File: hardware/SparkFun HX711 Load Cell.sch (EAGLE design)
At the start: 27 parts, among them Q1 MMBT4403, U1 HX711, U7 OSHW-LOGOS

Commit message: Fixing issues #6.
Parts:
- FRAME1: value FRAME-LETTER -> (none); DESIGNER (none) -> N. Seidle; VERSION (none) -> v10
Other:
- note removed: "20k 8.2k"
- note removed: "N. Seidle"
- note removed: "v01"
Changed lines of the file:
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@@
 </classes>
 <parts>
-<part name="FRAME1" library="SparkFun-Aesthetics" deviceset="FRAME-LETTER" device=""/>
 <part name="U7" library="SparkFun-Aesthetics" deviceset="OSHW-LOGO" device="S"/>
 <part name="STANDOFF1" library="SparkFun-Electromechanical" deviceset="STAND-OFF" device=""/>
@@
 <part name="GND6" library="SparkFun-Aesthetics" deviceset="GND" device=""/>
 <part name="GND9" library="SparkFun-Aesthetics" deviceset="GND" device=""/>
+<part name="FRAME1" library="SparkFun-Aesthetics" deviceset="FRAME-LETTER" device="">
+<attribute name="DESIGNER" value="N. Seidle"/>
+<attribute name="VERSION" value="v10"/>
+</part>
 </parts>
 <sheets>
@@
 <text x="10.414" y="128.016" size="1.778" layer="97">Common Load
 Cell Colors:</text>
-<text x="172.72" y="10.16" size="2.54" layer="94">N. Seidle</text>
-<text x="238.76" y="7.62" size="2.54" layer="94">v01</text>
 <text x="213.36" y="99.06" size="1.778" layer="97">IO: 2.7-5.5V</text>
 <text x="38.1" y="114.3" size="1.778" layer="97">Shield</text>
@@
 <wire x1="36.576" y1="127" x2="40.64" y2="127" width="0.2032" layer="97"/>
 <wire x1="36.576" y1="113.03" x2="40.64" y2="113.03" width="0.2032" layer="97"/>
-<text x="63.5" y="144.78" size="1.778" layer="91">20k 8.2k</text>
 </plain>
 <instances>
-<instance part="FRAME1" gate="G$1" x="0" y="0"/>
-<instance part="FRAME1" gate="G$2" x="147.32" y="0"/>
 <instance part="U7" gate="G$1" x="132.08" y="12.7"/>
 <instance part="STANDOFF1" gate="G$1" x="243.84" y="38.1"/>
@@
 <instance part="GND6" gate="1" x="91.44" y="109.22"/>
 <instance part="GND9" gate="1" x="119.38" y="88.9"/>
+<instance part="FRAME1" gate="G$1" x="0" y="0"/>
+<instance part="FRAME1" gate="V" x="147.32" y="0"/>
 </instances>
 <busses>

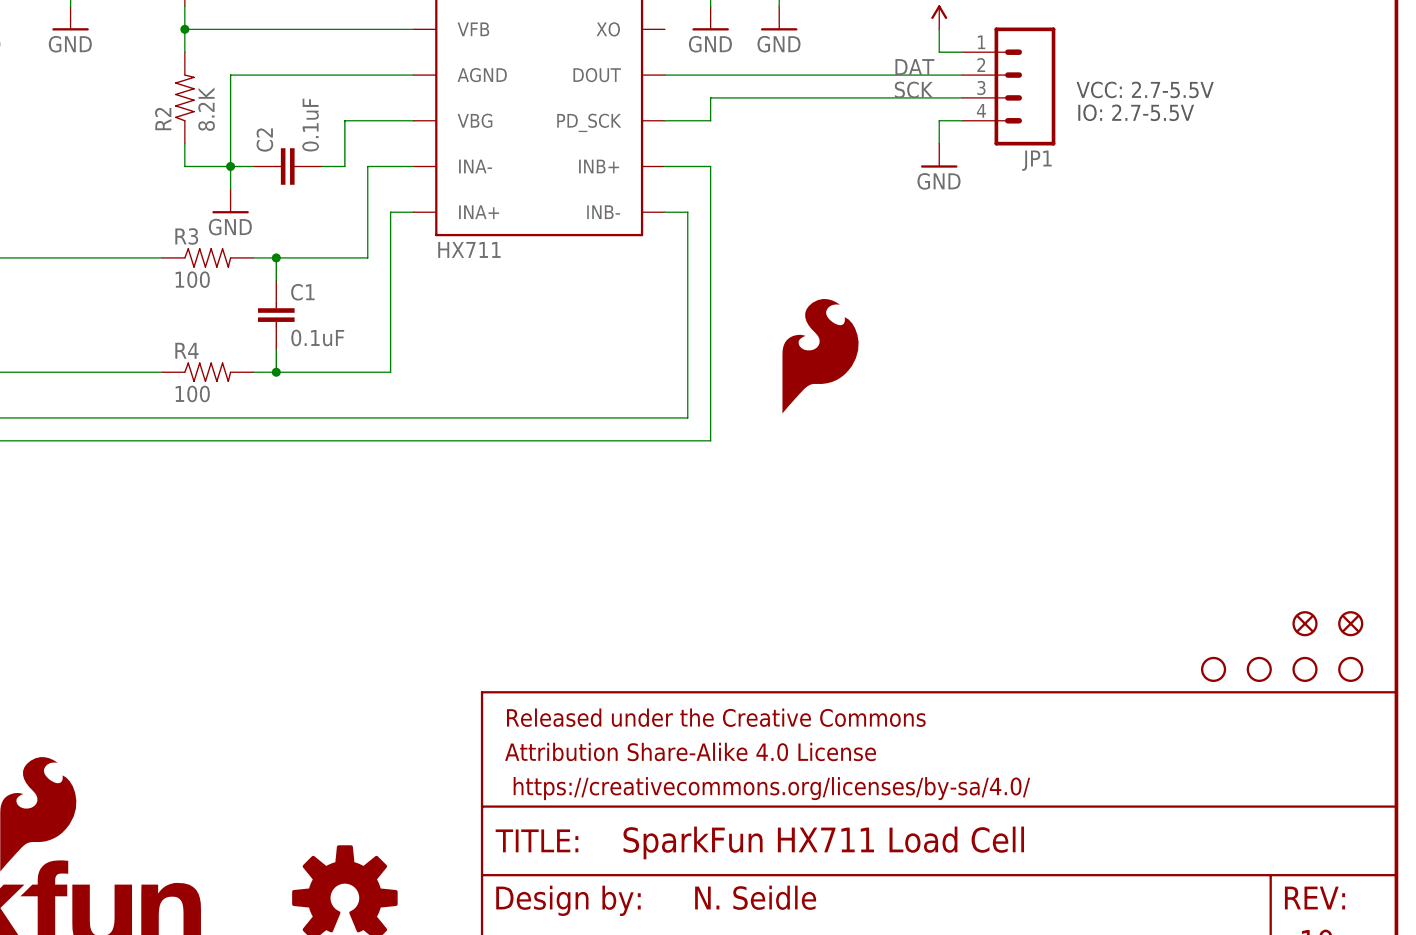
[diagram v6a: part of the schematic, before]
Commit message: Fixed feedback from eng review.
Moved VCC trace out of tKeepout. Fixed 4-way junction on schematic.
Moved schematic part for standoff holes to proper location.
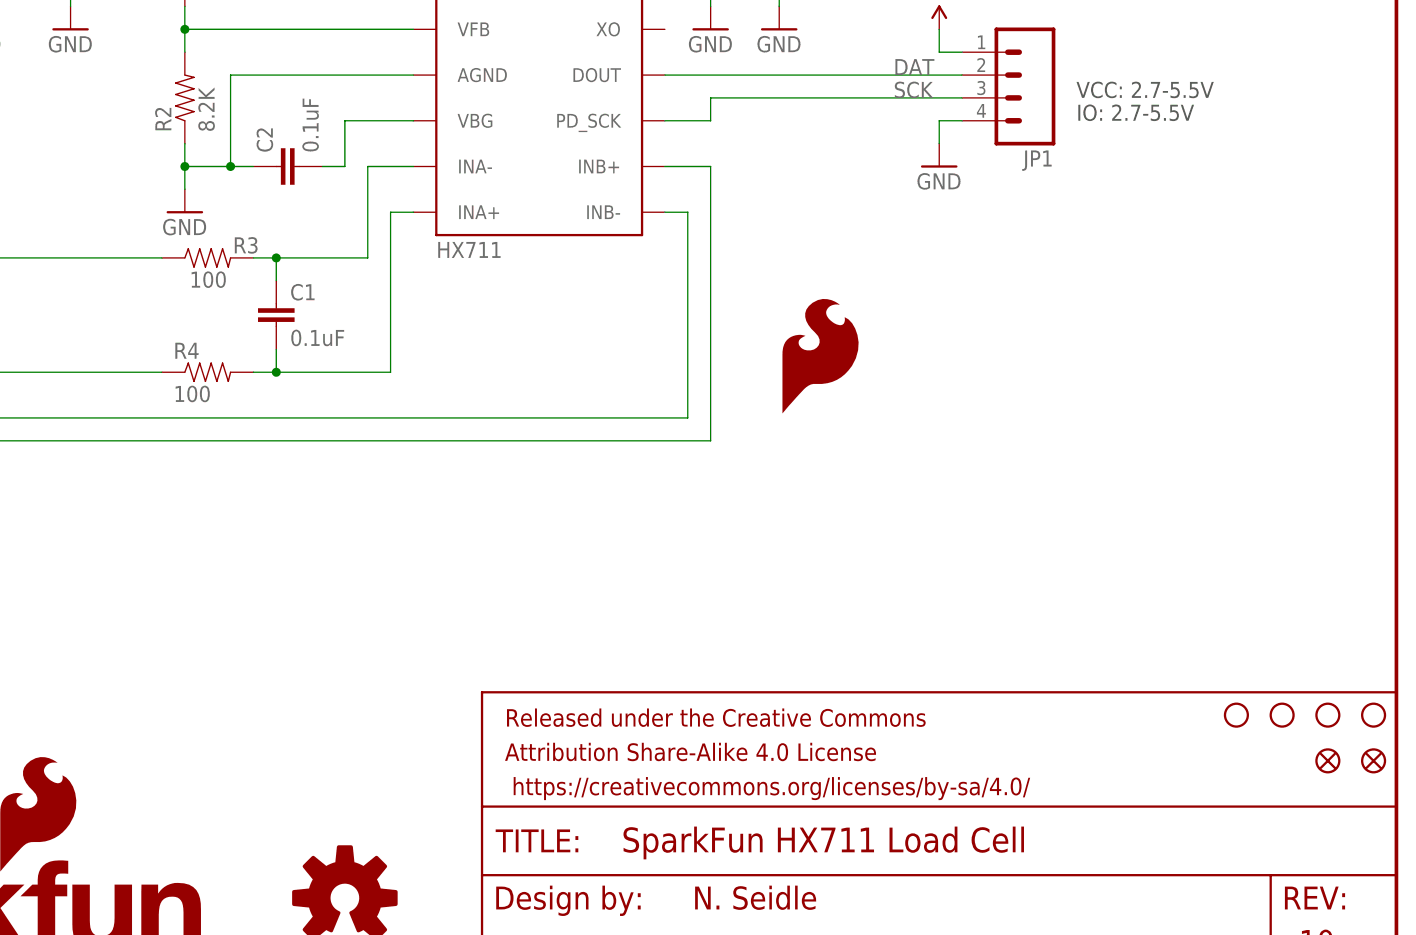
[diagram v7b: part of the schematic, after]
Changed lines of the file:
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@@
 <?xml version="1.0" encoding="utf-8"?>
 <!DOCTYPE eagle SYSTEM "eagle.dtd">
-<eagle version="7.1.0">
+<eagle version="7.2.0">
 <drawing>
 <settings>
@@
 <layer number="255" name="routoute" color="7" fill="1" visible="yes" active="yes"/>
 </layers>
-<schematic xreflabel="%F%N/%S.%C%R" xrefpart="/%S.%C%R">
+<schematic xreflabel="%F%N/%S" xrefpart="/%S.%C%R">
 <attributes>
 </attributes>
@@
 <instances>
 <instance part="U7" gate="G$1" x="132.08" y="12.7"/>
-<instance part="STANDOFF1" gate="G$1" x="243.84" y="38.1"/>
-<instance part="STANDOFF2" gate="G$1" x="238.76" y="38.1"/>
-<instance part="STANDOFF3" gate="G$1" x="233.68" y="38.1"/>
-<instance part="STANDOFF4" gate="G$1" x="228.6" y="38.1"/>
+<instance part="STANDOFF1" gate="G$1" x="246.38" y="33.02"/>
+<instance part="STANDOFF2" gate="G$1" x="241.3" y="33.02"/>
+<instance part="STANDOFF3" gate="G$1" x="236.22" y="33.02"/>
+<instance part="STANDOFF4" gate="G$1" x="231.14" y="33.02"/>
 <instance part="LOGO1" gate="G$1" x="60.96" y="2.54"/>
 <instance part="JP1" gate="G$1" x="205.74" y="104.14" rot="R180"/>
@@
 <instance part="Q1" gate="G$1" x="121.92" y="132.08" rot="MR0"/>
 <instance part="GND1" gate="1" x="198.12" y="93.98"/>
-<instance part="R3" gate="G$1" x="116.84" y="83.82"/>
+<instance part="R3" gate="G$1" x="116.84" y="83.82" smashed="yes">
+<attribute name="NAME" x="119.634" y="84.328" size="1.778" layer="95"/>
+<attribute name="VALUE" x="114.808" y="80.518" size="1.778" layer="96"/>
+</instance>
 <instance part="R4" gate="G$1" x="116.84" y="71.12"/>
 <instance part="C6" gate="G$1" x="106.68" y="144.78"/>
@@
 <instance part="GND8" gate="1" x="91.44" y="137.16"/>
 <instance part="LOGO3" gate="G$1" x="180.34" y="66.04"/>
-<instance part="FID1" gate="G$1" x="243.84" y="43.18"/>
-<instance part="FID2" gate="G$1" x="238.76" y="43.18"/>
+<instance part="FID1" gate="G$1" x="246.38" y="27.94"/>
+<instance part="FID2" gate="G$1" x="241.3" y="27.94"/>
 <instance part="JP2" gate="G$1" x="50.8" y="99.06"/>
 <instance part="SJ2" gate="G$1" x="180.34" y="119.38" rot="R90"/>
@@
 <instance part="C3" gate="G$1" x="91.44" y="116.84"/>
 <instance part="GND6" gate="1" x="91.44" y="109.22"/>
-<instance part="GND9" gate="1" x="119.38" y="88.9"/>
+<instance part="GND9" gate="1" x="114.3" y="88.9"/>
 <instance part="FRAME1" gate="G$1" x="0" y="0"/>
 <instance part="FRAME1" gate="V" x="147.32" y="0"/>
@@
 <pinref part="C2" gate="G$1" pin="1"/>
 <pinref part="GND9" gate="1" pin="GND"/>
-<wire x1="119.38" y1="93.98" x2="119.38" y2="91.44" width="0.1524" layer="91"/>
-</segment>
-<segment>
+<wire x1="114.3" y1="91.44" x2="114.3" y2="93.98" width="0.1524" layer="91"/>
+<junction x="114.3" y="93.98"/>
+</segment>
+<segment>

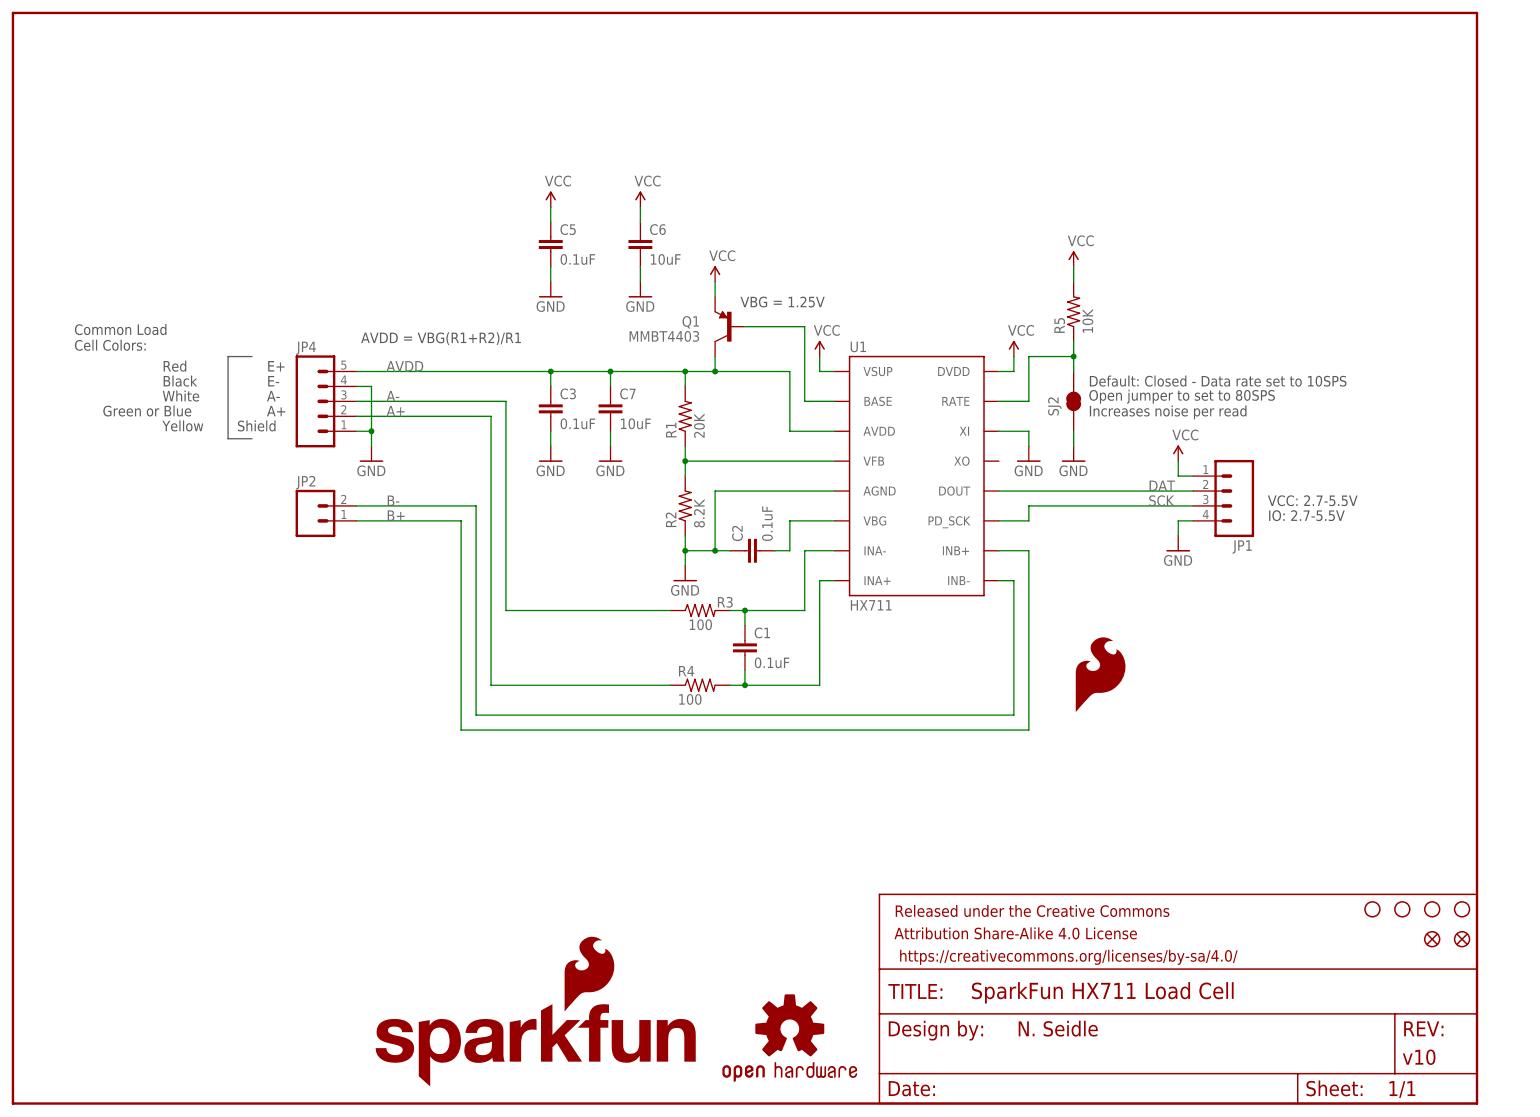
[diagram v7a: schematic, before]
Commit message: Revision 11 changes
-Added 3.3uH inductor, this should allow for greater resolution in the
HX711 ADC.
-Separated analog and digital supply voltage, which allows 3.3V uCs to
communicate without additional hardware.
-Added 0.1uF cap to digital supply.
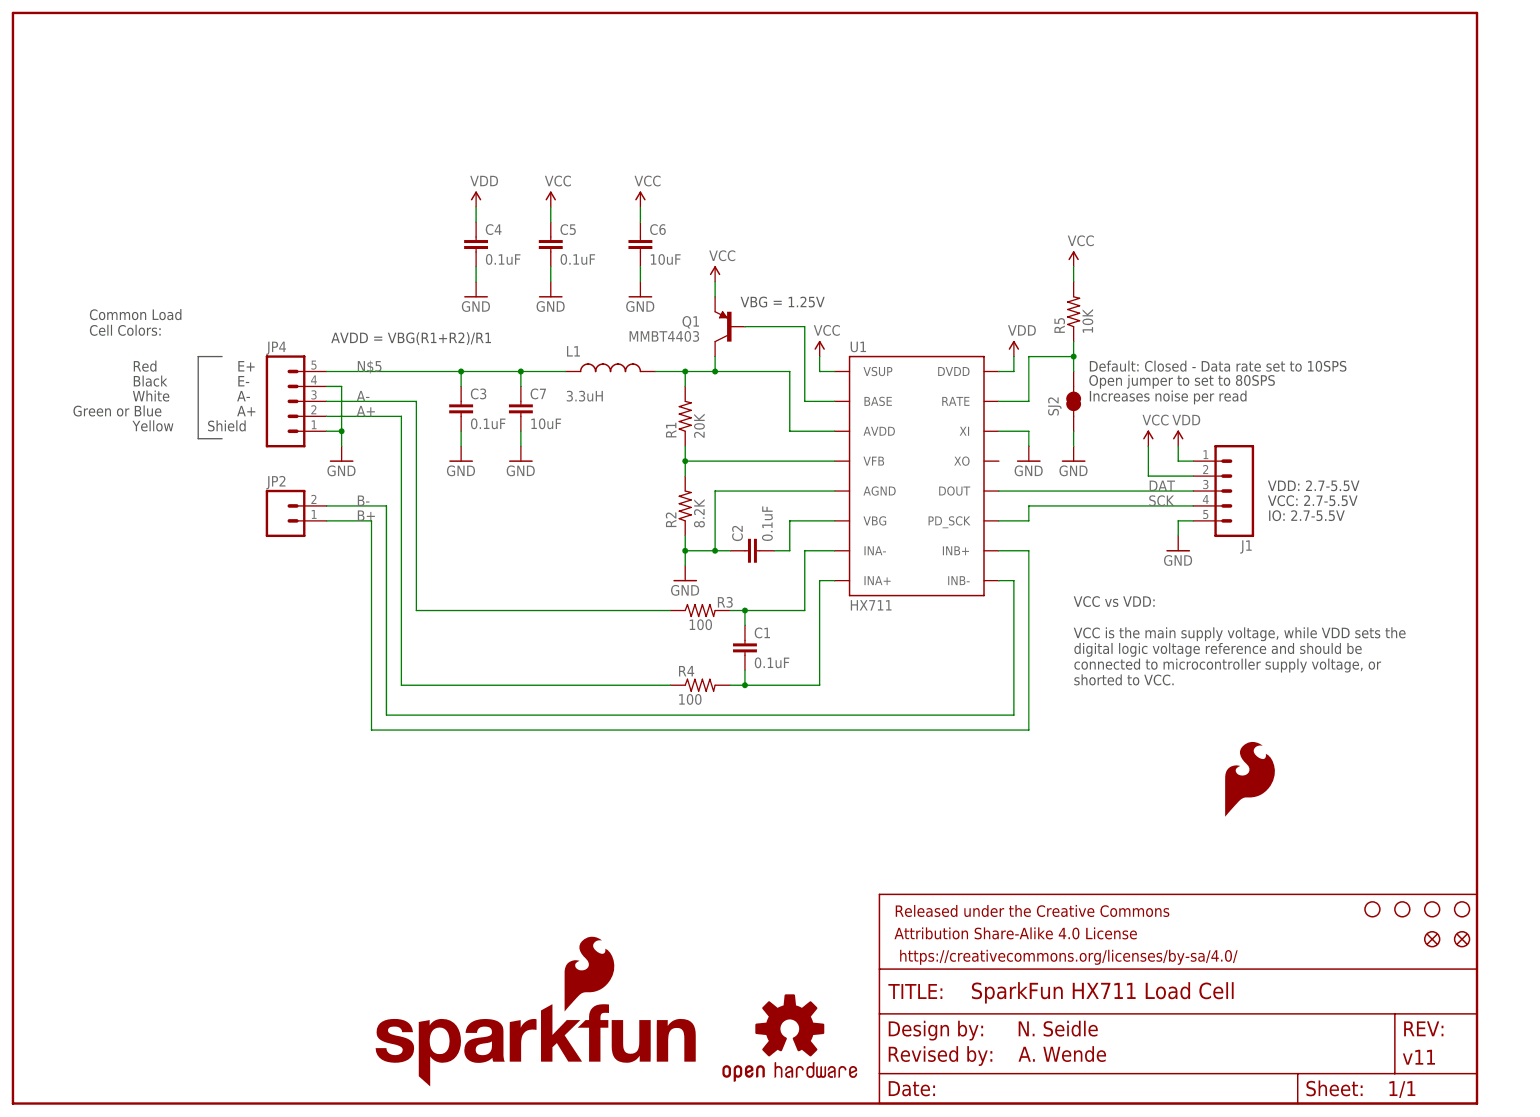
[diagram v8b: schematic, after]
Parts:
- removed JP1: (no value), SparkFun-Connectors:M04PTH
- added C4: 0.1uF, SparkFun-Capacitors:0.1UF-25V-5%(0603)
- added J1: (no value), SparkFun-Connectors:M05PTH
- added L1: 3.3uH, SparkFun-Passives:INDUCTOR0805-IND
- FRAME1: VERSION v10 -> v11
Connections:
- new net N$5: C3.1, C7.1, JP4.5, L1.1
- new net VDD: C4.1, J1.1, U1.DVDD
- net AVDD: now also L1.2; no longer C3.1, C7.1, JP4.5
- net DAT: now also J1.3; no longer JP1.2
- net GND: now also C4.2, J1.5; no longer JP1.4
- net SCK: now also J1.4; no longer JP1.3
- net VCC: now also J1.2; no longer JP1.1, U1.DVDD
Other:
- note added: "A. Wende"
- note added: "Revised by:"
- note added: "VCC vs VDD: VCC is the main supply voltage, while VDD sets the digital logic voltage reference and should be connected to microcontroller supply voltage, or shorted to VCC."
- note added: "VDD: 2.7-5.5V"
- moved on the sheet: C3, C7, JP2, JP4
